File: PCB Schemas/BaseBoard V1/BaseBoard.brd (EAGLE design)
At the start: 94 x 31.1 mm, 31 parts, among them IC1 74HC595D, IC2 74HC595D, IC3 74HC595D, U1 ATMEGA2560AU, X1 16MHz

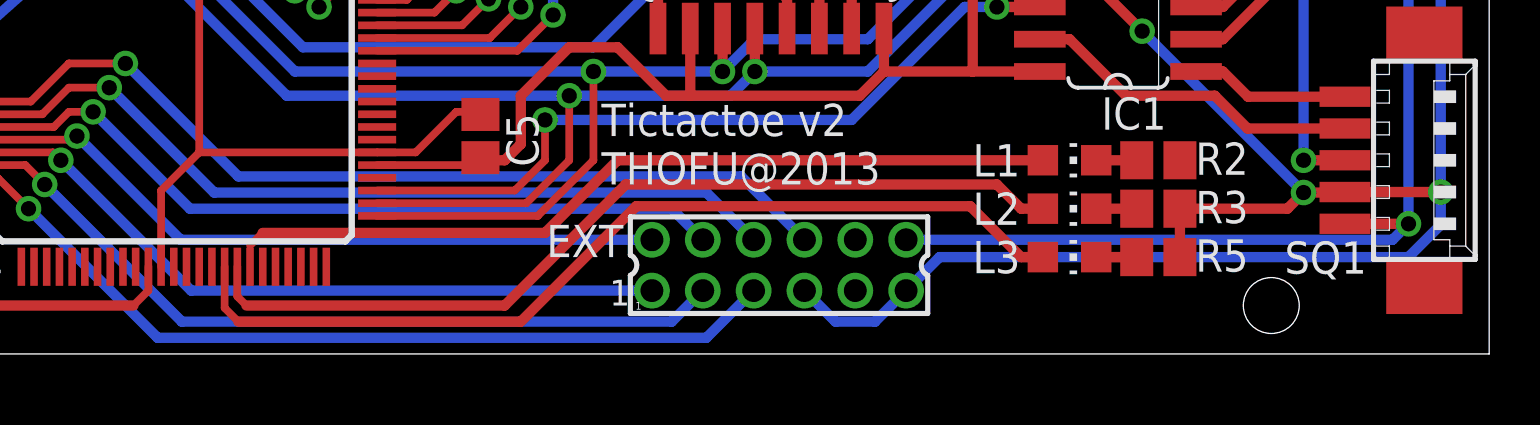
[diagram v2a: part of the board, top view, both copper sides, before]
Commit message: Update base conector package
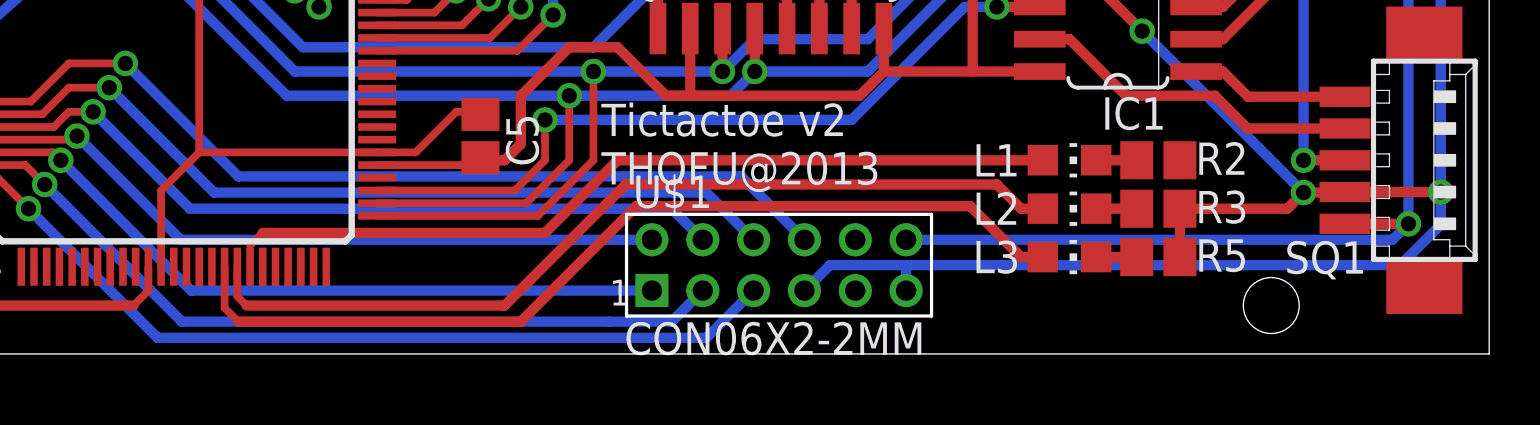
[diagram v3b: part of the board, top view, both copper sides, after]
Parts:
- removed EXT: 87758-1216, con-molex:87758-1216
- added U$1: CON06X2-2MM, Connectors:CON06X2_2MM
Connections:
- net +3.3V: now also U$1.10; no longer EXT.10
- net +VIN: now also U$1.9; no longer EXT.9
- net BASE_RX: now also U$1.1; no longer EXT.1
- net BASE_TX: now also U$1.3; no longer EXT.3
- net GND: now also U$1.11, U$1.7; no longer EXT.11, EXT.7
- net INT_BUTTONS: now also U$1.8; no longer EXT.8
- net INT_EXT: now also U$1.5; no longer EXT.5
- net INT_RFID: now also U$1.6; no longer EXT.6
- net SCL: now also U$1.4; no longer EXT.4
- net SDA: now also U$1.2; no longer EXT.2
- net VCC: now also U$1.12; no longer EXT.12

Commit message: Updated details
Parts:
- C1: value 22pF -> 100nF
- C3: value 100nF -> 22pF
- IC1: value 74HC595D -> ATMEGA2560AU; device 74xx-eu:SO16 -> SparkFun-DigitalIC:TQFP100
- J1: value (none) -> PROGRAM
- J2: value CON06X2-2MM -> (none)
- U1: value ATMEGA2560AU -> 74HC595D; device SparkFun-DigitalIC:TQFP100 -> 74xx-eu:SO16
- moved R2 53.2 mm to (27.9, 3.81)
- moved R4 53.1 mm to (81.0, 5.71)
- moved IC1 37.4 mm to (42.2, 11.4), turned to 270 degrees
- moved U1 37.4 mm to (79.4, 15.6), turned to 90 degrees
- moved C1 15.6 mm to (8.26, 4.45), turned to 0 degrees
- moved C3 15.6 mm to (22.5, 10.8), turned to 270 degrees
- moved L1 3.81 mm to (77.5, 3.81)
- moved L3 3.81 mm to (77.5, 7.62)
- moved R5 3.81 mm to (81.0, 7.62)
- moved R3 1.90 mm to (81.0, 3.81)
- renumbered IC2 to U2, IC3 to U3, PROG to J1, SQ1 to S1, SQ2 to S2, SQ3 to S3, SQ4 to S4, SQ5 to S5, SQ6 to S6, SQ7 to S7, SQ8 to S8, SQ9 to S9, U$1 to J2
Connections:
- removed net N$4 (its old number): L1.C, R2.1
- new net N$9: L1.C, R3.1
- net +VIN: now also J2.7; no longer J2.9
- net AREF: now also IC1.98; no longer U1.98
- net BASE_RX: now also IC1.45; no longer U1.45
- net BASE_TX: now also IC1.46; no longer U1.46
- net CLK: now also IC1.76, U1.11; no longer IC1.11, U1.76
- net COL1: now also IC1.89; no longer U1.89
- net COL2: now also IC1.90; no longer U1.90
- net COL3: now also IC1.91; no longer U1.91
- net COL4: now also IC1.92; no longer U1.92
- net COL5: now also IC1.93; no longer U1.93
- net COL6: now also IC1.94; no longer U1.94
- net COL7: now also IC1.95; no longer U1.95
- net COL8: now also IC1.96; no longer U1.96
- net COL9: now also IC1.97; no longer U1.97
- net DATA: now also IC1.78, U1.14; no longer IC1.14, U1.78
- net DBG1: now also IC1.67, L1.A; no longer L3.A, U1.67
- net DBG2: now also IC1.68; no longer U1.68
- net DBG3: now also IC1.69, L3.A; no longer L1.A, U1.69
- net GND: now also C3.1, IC1.11, IC1.32, IC1.62, IC1.81, IC1.99, J2.9, U1.13, U1.8; no longer C1.1, IC1.13, IC1.8, J2.7, U1.11, U1.32, U1.62, U1.81, U1.99
- net GR1: now also U1.15; no longer IC1.15
- net GR2: now also U1.2; no longer IC1.2
- net GR3: now also U1.4; no longer IC1.4
- net INT_BUTTONS: now also IC1.41; no longer U1.41
- net INT_EXT: now also IC1.47; no longer U1.47
- net INT_RFID: now also IC1.42; no longer U1.42
- net LATCH: now also IC1.77, U1.12; no longer IC1.12, U1.77
- net MISO: now also IC1.22; no longer U1.22
- net MOSI: now also IC1.21; no longer U1.21
- net N$1: now also IC1.33; no longer U1.33
- net N$2: now also C3.2, IC1.34; no longer C1.2, U1.34
- net N$3: now also R4.1; no longer R3.1
- net N$5: now also C1.1; no longer C3.1
- net N$6: now also U1.9; no longer IC1.9
- net N$8: now also R2.1; no longer R4.1
- net RED1: now also U1.1; no longer IC1.1
- net RED2: now also U1.3; no longer IC1.3
- net RED3: now also U1.5; no longer IC1.5
- net RESET: now also C1.2, IC1.30; no longer C3.2, U1.30
- net RX: now also IC1.2; no longer U1.2
- net SCK: now also IC1.20; no longer U1.20
- net SCL: now also IC1.43; no longer U1.43
- net SDA: now also IC1.44; no longer U1.44
- net TX: now also IC1.3; no longer U1.3
- net VCC: now also IC1.100, IC1.31, IC1.61, IC1.80, U1.16; no longer IC1.16, U1.100, U1.31, U1.61, U1.80
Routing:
- net N$9: track 0.00 -> 1.59 mm
- net N$4 (its old number): track 1.59 -> 0.00 mm
- net GND: track 381.5 -> 380.4 mm
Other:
- board text added: "Tictactoe v2.1 THOFU@2013"
- board text removed: "1"
- board text removed: "Tictactoe v2 THOFU@2013"

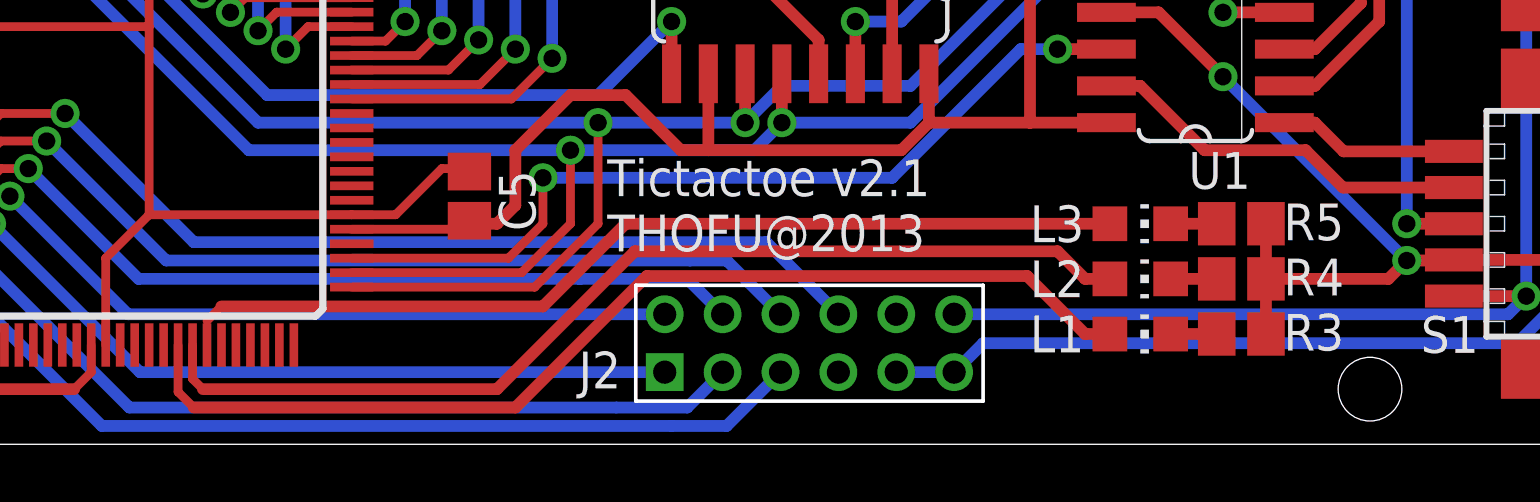
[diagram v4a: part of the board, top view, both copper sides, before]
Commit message: Changed debug pins
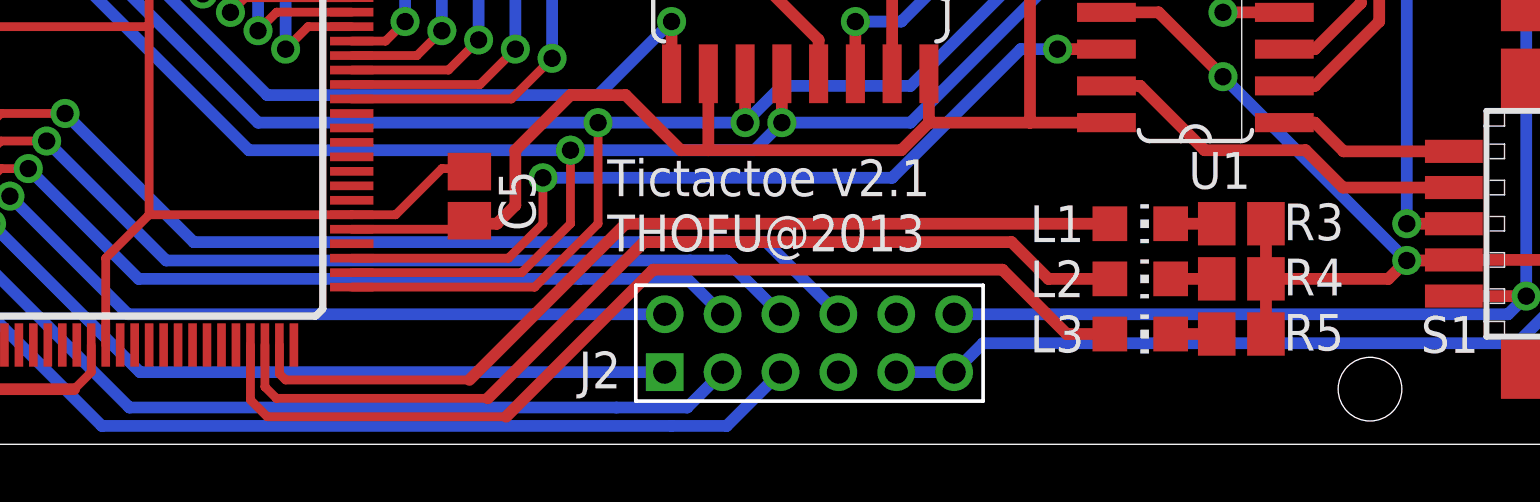
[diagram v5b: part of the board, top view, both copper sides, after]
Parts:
- moved L1 3.81 mm to (77.5, 7.62)
- moved L3 3.81 mm to (77.5, 3.81)
- moved R3 3.81 mm to (81.0, 7.62)
- moved R5 3.81 mm to (81.0, 3.81)
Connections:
- net DBG1: now also IC1.74; no longer IC1.67
- net DBG2: now also IC1.73; no longer IC1.68
- net DBG3: now also IC1.72; no longer IC1.69
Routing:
- net DBG1: track 36.7 -> 32.0 mm
- net DBG3: track 32.6 -> 34.9 mm
- net DBG2: track 35.4 -> 33.6 mm
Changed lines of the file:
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@@
 <attribute name="VALUE" x="27.178" y="1.524" size="1.27" layer="27"/>
 </element>
-<element name="R3" library="resistor" package="R0805" value="330" x="80.9625" y="3.81" smashed="yes">
+<element name="R3" library="resistor" package="R0805" value="330" x="80.9625" y="7.62" smashed="yes">
+<attribute name="NAME" x="82.423" y="7.0485" size="1.27" layer="25"/>
+<attribute name="VALUE" x="80.2005" y="5.334" size="1.27" layer="27"/>
+</element>
+<element name="ICSP" library="SparkFun-Connectors" package="2X3-NS" value="AVR_SPI_PRG_6NS" x="16.1925" y="5.3975" rot="R180"/>
+<element name="R5" library="resistor" package="R0805" value="330" x="80.9625" y="3.81" smashed="yes">
 <attribute name="NAME" x="82.423" y="3.2385" size="1.27" layer="25"/>
 <attribute name="VALUE" x="80.2005" y="1.524" size="1.27" layer="27"/>
-</element>
-<element name="ICSP" library="SparkFun-Connectors" package="2X3-NS" value="AVR_SPI_PRG_6NS" x="16.1925" y="5.3975" rot="R180"/>
-<element name="R5" library="resistor" package="R0805" value="330" x="80.9625" y="7.62" smashed="yes">
-<attribute name="NAME" x="82.423" y="7.0485" size="1.27" layer="25"/>
-<attribute name="VALUE" x="80.2005" y="5.334" size="1.27" layer="27"/>
 </element>
 <element name="R4" library="resistor" package="R0805" value="330" x="80.9625" y="5.715" smashed="yes">
@@
 <attribute name="VALUE" x="76.2" y="3.175" size="1.27" layer="27"/>
 </element>
-<element name="L3" library="led" package="CHIP-LED0805" value="" x="77.47" y="7.62" smashed="yes" rot="R270">
+<element name="L3" library="led" package="CHIP-LED0805" value="" x="77.47" y="3.81" smashed="yes" rot="R270">
+<attribute name="NAME" x="73.66" y="3.175" size="1.27" layer="25"/>
+<attribute name="VALUE" x="76.2" y="1.27" size="1.27" layer="27"/>
+</element>
+<element name="L1" library="led" package="CHIP-LED0805" value="" x="77.47" y="7.62" smashed="yes" rot="R270">
 <attribute name="NAME" x="73.66" y="6.985" size="1.27" layer="25"/>
 <attribute name="VALUE" x="76.2" y="5.08" size="1.27" layer="27"/>
-</element>
-<element name="L1" library="led" package="CHIP-LED0805" value="" x="77.47" y="3.81" smashed="yes" rot="R270">
-<attribute name="NAME" x="73.66" y="3.175" size="1.27" layer="25"/>
-<attribute name="VALUE" x="76.2" y="1.27" size="1.27" layer="27"/>
 </element>
 <element name="J2" library="Connectors" package="CON06X2_2MM" value="" x="66.04" y="3.4925" smashed="yes">
@@
 <wire x1="80.3275" y1="12.7" x2="86.6775" y2="6.35" width="0.4064" layer="16"/>
 <contactref element="R4" pad="2"/>
-<wire x1="81.8125" y1="3.81" x2="81.8125" y2="5.715" width="0.4064" layer="1"/>
 <wire x1="86.6775" y1="6.35" x2="86.0425" y2="5.715" width="0.4064" layer="1"/>
-<wire x1="86.0425" y1="5.715" x2="81.8125" y2="5.715" width="0.4064" layer="1"/>
 <wire x1="4.445" y1="16.8275" x2="4.445" y2="13.0175" width="0.4064" layer="16"/>
 <wire x1="4.445" y1="13.0175" x2="1.5875" y2="10.16" width="0.4064" layer="16"/>
@@
 <wire x1="90.4875" y1="3.4925" x2="72.04" y2="3.4925" width="0.4064" layer="16"/>
 <wire x1="72.04" y1="3.4925" x2="71.04" y2="2.4925" width="0.4064" layer="16"/>
+<wire x1="86.0425" y1="5.715" x2="81.8125" y2="5.715" width="0.4064" layer="1"/>
 <wire x1="81.8125" y1="7.62" x2="81.8125" y2="5.715" width="0.4064" layer="1"/>
+<wire x1="81.8125" y1="5.715" x2="81.8125" y2="3.81" width="0.4064" layer="1"/>
 </signal>
 <signal name="VCC">
@@
 <contactref element="R3" pad="1"/>
 <contactref element="L1" pad="C"/>
-<wire x1="78.52" y1="3.81" x2="80.1125" y2="3.81" width="0.4064" layer="1"/>
+<wire x1="78.52" y1="7.62" x2="80.1125" y2="7.62" width="0.4064" layer="1"/>
 </signal>
 <signal name="DBG2">
 <contactref element="L2" pad="A"/>
-<contactref element="IC1" pad="68"/>
-<wire x1="44.7275" y1="3.43" x2="44.7275" y2="2.2625" width="0.3048" layer="1"/>
-<wire x1="44.7275" y1="2.2625" x2="45.085" y2="1.905" width="0.3048" layer="1"/>
-<wire x1="60.0075" y1="6.6675" x2="55.245" y2="1.905" width="0.4064" layer="1"/>
-<wire x1="55.245" y1="1.905" x2="45.085" y2="1.905" width="0.4064" layer="1"/>
-<wire x1="60.0075" y1="6.6675" x2="74.6125" y2="6.6675" width="0.4064" layer="1"/>
-<wire x1="74.6125" y1="6.6675" x2="75.565" y2="5.715" width="0.4064" layer="1"/>
-<wire x1="75.565" y1="5.715" x2="76.42" y2="5.715" width="0.4064" layer="1"/>
+<contactref element="IC1" pad="73"/>
+<wire x1="76.42" y1="5.715" x2="74.295" y2="5.715" width="0.4064" layer="1"/>
+<wire x1="74.295" y1="5.715" x2="73.025" y2="6.985" width="0.4064" layer="1"/>
+<wire x1="73.025" y1="6.985" x2="60.325" y2="6.985" width="0.4064" layer="1"/>
+<wire x1="60.325" y1="6.985" x2="54.9275" y2="1.5875" width="0.4064" layer="1"/>
+<wire x1="47.2275" y1="3.43" x2="47.2275" y2="1.985" width="0.3048" layer="1"/>
+<wire x1="47.2275" y1="1.985" x2="47.625" y2="1.5875" width="0.3048" layer="1"/>
+<wire x1="47.625" y1="1.5875" x2="54.9275" y2="1.5875" width="0.3048" layer="1"/>
 </signal>
 <signal name="DBG3">
 <contactref element="L3" pad="A"/>
-<wire x1="59.69" y1="7.62" x2="76.42" y2="7.62" width="0.4064" layer="1"/>
-<wire x1="45.2275" y1="4.27" x2="45.72" y2="4.7625" width="0.3048" layer="1"/>
-<wire x1="45.72" y1="4.7625" x2="56.8325" y2="4.7625" width="0.4064" layer="1"/>
-<wire x1="56.8325" y1="4.7625" x2="59.69" y2="7.62" width="0.4064" layer="1"/>
-<contactref element="IC1" pad="69"/>
-<wire x1="45.2275" y1="3.43" x2="45.2275" y2="4.27" width="0" layer="19" extent="1-1"/>
+<contactref element="IC1" pad="72"/>
+<wire x1="76.42" y1="3.81" x2="74.93" y2="3.81" width="0.4064" layer="1"/>
+<wire x1="74.93" y1="3.81" x2="72.7075" y2="6.0325" width="0.4064" layer="1"/>
+<wire x1="72.7075" y1="6.0325" x2="60.6425" y2="6.0325" width="0.4064" layer="1"/>
+<wire x1="60.6425" y1="6.0325" x2="55.5625" y2="0.9525" width="0.4064" layer="1"/>
+<wire x1="46.7275" y1="3.43" x2="46.7275" y2="1.5325" width="0.3048" layer="1"/>
+<wire x1="46.7275" y1="1.5325" x2="47.3075" y2="0.9525" width="0.3048" layer="1"/>
+<wire x1="47.3075" y1="0.9525" x2="55.5625" y2="0.9525" width="0.3048" layer="1"/>
 </signal>
 <signal name="RED4">
@@
 <signal name="DBG1">
 <contactref element="L1" pad="A"/>
-<contactref element="IC1" pad="67"/>
-<wire x1="44.2275" y1="3.43" x2="44.2275" y2="1.81" width="0.3048" layer="1"/>
-<wire x1="44.2275" y1="1.81" x2="44.7675" y2="1.27" width="0.3048" layer="1"/>
-<wire x1="60.4225" y1="5.8125" x2="55.88" y2="1.27" width="0.4064" layer="1"/>
-<wire x1="55.88" y1="1.27" x2="44.7675" y2="1.27" width="0.4064" layer="1"/>
-<wire x1="60.4225" y1="5.8125" x2="73.5625" y2="5.8125" width="0.4064" layer="1"/>
-<wire x1="73.5625" y1="5.8125" x2="75.565" y2="3.81" width="0.4064" layer="1"/>
-<wire x1="75.565" y1="3.81" x2="76.42" y2="3.81" width="0.4064" layer="1"/>
+<contactref element="IC1" pad="74"/>
+<wire x1="76.42" y1="7.62" x2="59.69" y2="7.62" width="0.4064" layer="1"/>
+<wire x1="59.69" y1="7.62" x2="54.2925" y2="2.2225" width="0.4064" layer="1"/>
+<wire x1="47.7275" y1="3.43" x2="47.7275" y2="2.4375" width="0.3048" layer="1"/>
+<wire x1="47.7275" y1="2.4375" x2="47.9425" y2="2.2225" width="0.3048" layer="1"/>
+<wire x1="47.9425" y1="2.2225" x2="54.2925" y2="2.2225" width="0.3048" layer="1"/>
 </signal>
 <signal name="N$3">
@@
 <contactref element="R5" pad="1"/>
 <contactref element="L3" pad="C"/>
-<wire x1="78.52" y1="7.62" x2="80.1125" y2="7.62" width="0.4064" layer="1"/>
+<wire x1="78.52" y1="3.81" x2="80.1125" y2="3.81" width="0.4064" layer="1"/>
 </signal>
 <signal name="+3.3V">
